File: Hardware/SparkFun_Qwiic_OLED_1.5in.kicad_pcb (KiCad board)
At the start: 2 copper layers, 34.3 x 48.3 mm, 60 parts, among them J1 Qwiic_RA, J2 Qwiic_RA, J3 Conn_01x06, J4 Conn_01x24_FPC, U2 WEO128128ASAP3N00000, U5 AP3012

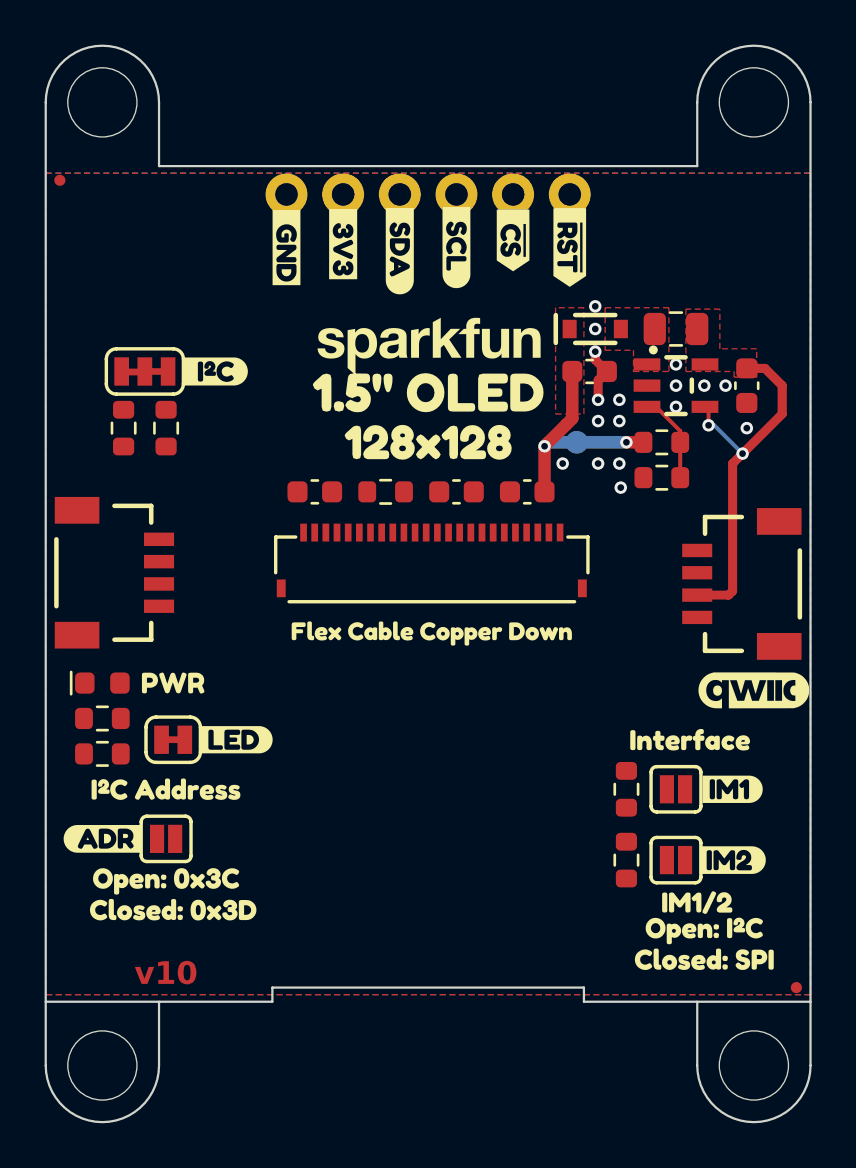
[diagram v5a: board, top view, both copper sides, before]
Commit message: Routes all traces
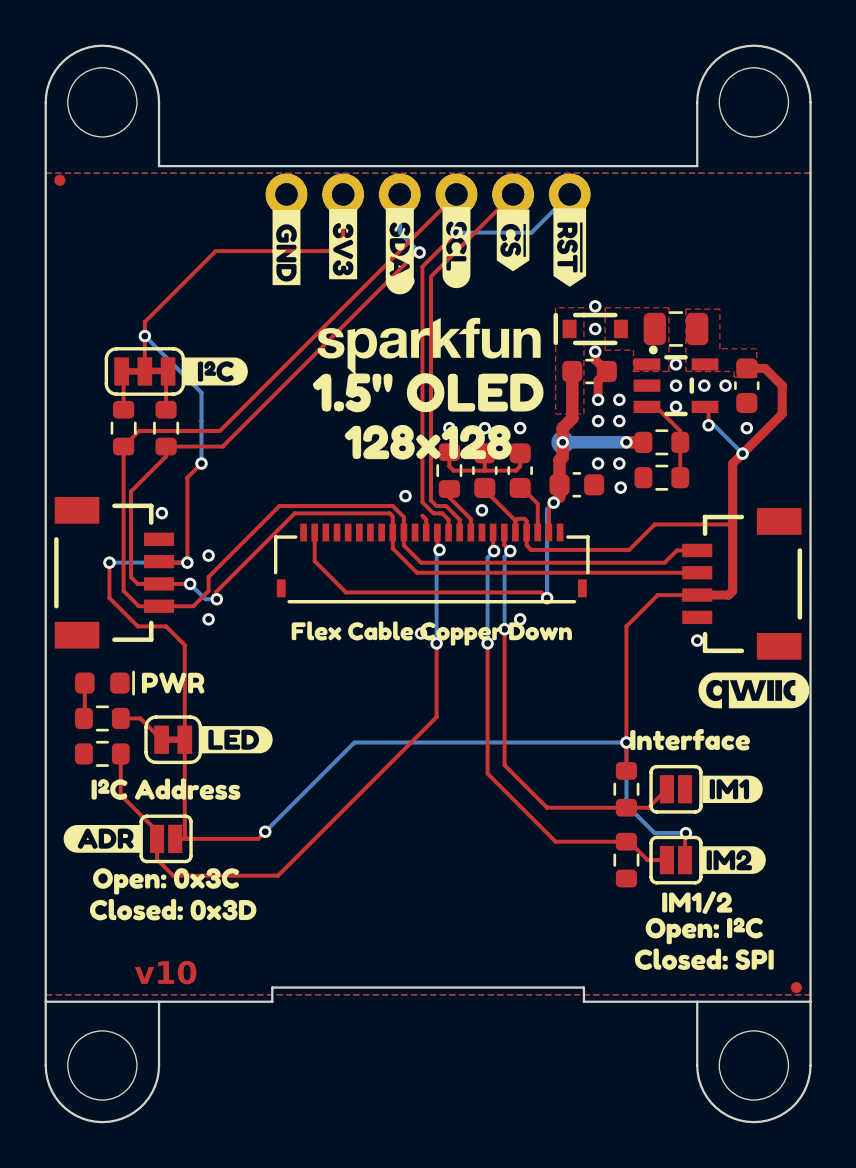
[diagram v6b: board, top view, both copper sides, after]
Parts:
- moved C3 9.26 mm to (144.5, 81.6), turned to 90 degrees
- moved R6 3.01 mm to (141.4, 81.6), turned to -90 degrees
- moved C5 2.25 mm to (147.1, 82.2), turned to 0 degrees
- moved R4 1.91 mm to (128.7, 79.7)
- moved R5 1.91 mm to (126.8, 79.7)
- moved C4 1.59 mm to (143.0, 81.6), turned to 90 degrees
- moved TP1 0.63 mm to (146.4, 80.3)
- turned D1 to 180 degrees
- turned JP2 to 0 degrees
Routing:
- net 3.3V: track 17.1 -> 116.1 mm, vias 2 -> 9
- net SCL/SCK: track 0.00 -> 56.3 mm
- net SDA/SDI: track 0.00 -> 54.1 mm, vias 0 -> 3
- net Net-(J4-Pin_13): track 0.00 -> 29.6 mm, vias 0 -> 2
- net Net-(J4-Pin_18): track 0.00 -> 20.6 mm, vias 0 -> 2
- net ~{RST}: track 0.00 -> 20.6 mm, vias 0 -> 1
- net Net-(J4-Pin_19): track 0.00 -> 19.1 mm, vias 0 -> 2
- net 12V: track 10.1 -> 28.1 mm, vias 2 -> 4
- net ~{CS}: track 0.00 -> 17.6 mm
- net GND: track 2.54 -> 9.07 mm, vias 17 -> 29
- net Net-(J4-Pin_22): track 0.00 -> 2.55 mm
- net Net-(J4-Pin_16): track 0.00 -> 2.35 mm
- net Net-(JP1-A): track 0.00 -> 2.22 mm
- net Net-(JP2-C): track 0.00 -> 1.75 mm
- net Net-(JP2-A): track 0.00 -> 1.75 mm
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
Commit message: Cleans up the routing
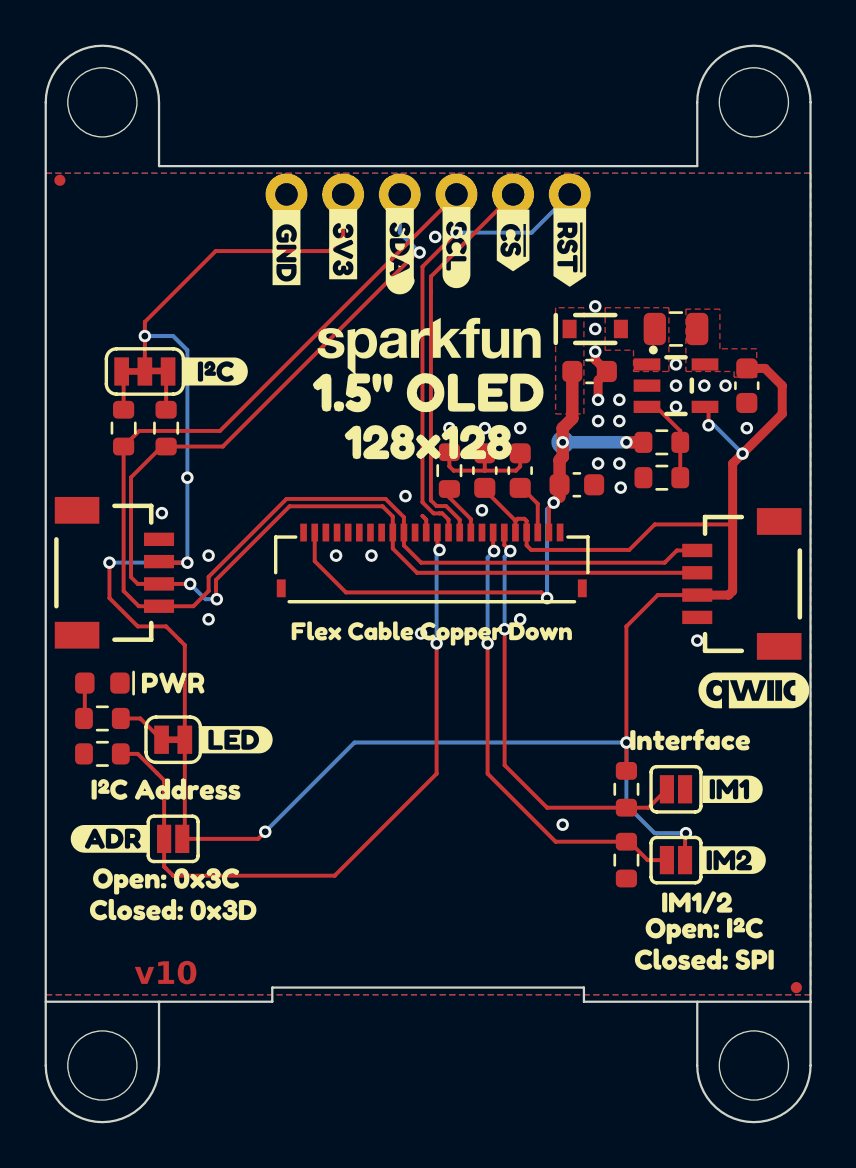
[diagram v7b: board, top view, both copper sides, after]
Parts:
- moved kibuzzard-68100A1E 0.32 mm to (126.1, 98.1)
- moved JP3 0.32 mm to (129.0, 98.1)
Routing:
- net Net-(J4-Pin_13): track 29.6 -> 31.5 mm
- net SDA/SDI: track 54.1 -> 54.8 mm
- net GND: vias 29 -> 33

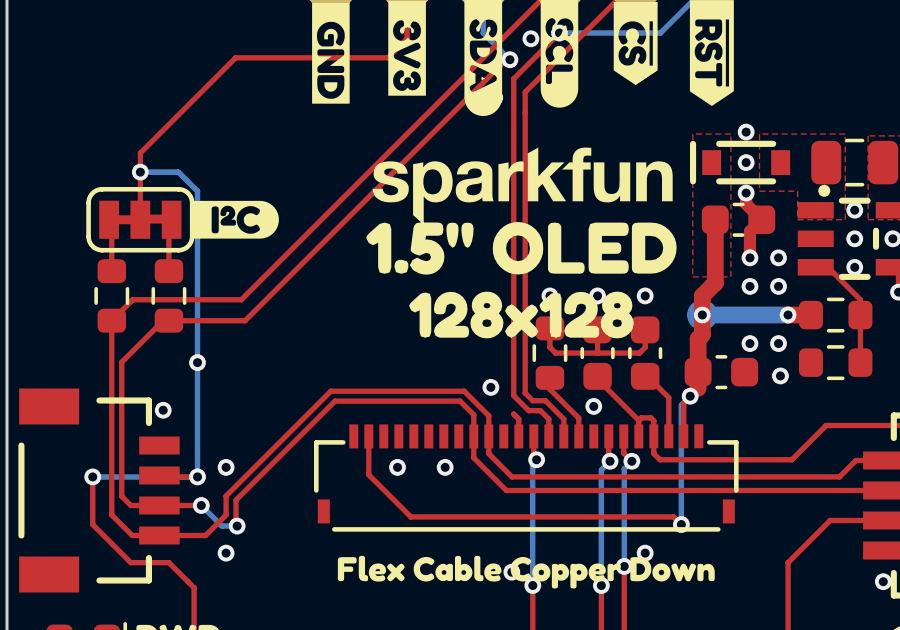
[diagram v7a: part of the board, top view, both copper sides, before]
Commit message: Moves some silk
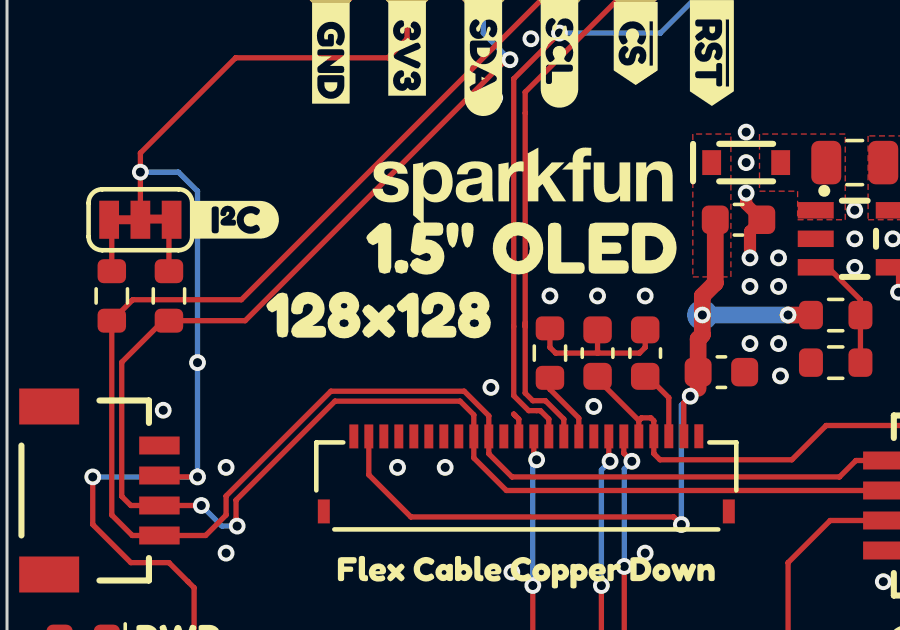
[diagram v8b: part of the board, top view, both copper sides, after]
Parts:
- moved kibuzzard-680FC73E 4.76 mm to (135.6, 80.3)
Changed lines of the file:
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@@
 	(footprint "kibuzzard-680FC73E"
 		(layer "F.Cu")
-		(at 140.411 80.326)
+		(at 135.6485 80.326)
 		(descr "Generated with KiBuzzard")
 		(tags "kb_params=eyJBbGlnbm1lbnRDaG9pY2UiOiAiQ2VudGVyIiwgIkNhcExlZnRDaG9pY2UiOiAiWyIsICJDYXBSaWdodENob2ljZSI6ICIpIiwgIkZvbnRDb21ib0JveCI6ICJGcmVkZHlTcGFyay1SZWd1bGFyIiwgIkhlaWdodEN0cmwiOiAxLjUsICJMYXllckNvbWJvQm94IjogIkYuU2lsa1MiLCAiTGluZVNwYWNpbmdDdHJsIjogMC4zLCAiTXVsdGlMaW5lVGV4dCI6ICIxMjh4MTI4IiwgIlBhZGRpbmdCb3R0b21DdHJsIjogMS4wLCAiUGFkZGluZ0xlZnRDdHJsIjogMi41LCAiUGFkZGluZ1JpZ2h0Q3RybCI6IDIuNSwgIlBhZGRpbmdUb3BDdHJsIjogMS4wLCAiV2lkdGhDdHJsIjogMC4zLCAiYWR2YW5jZWRDaGVja2JveCI6IHRydWUsICJpbmxpbmVGb3JtYXRUZXh0Ym94IjogdHJ1ZSwgImxpbmVvdmVyU3R5bGVDaG9pY2UiOiAiU3F1YXJlIiwgImxpbmVvdmVyVGhpY2tuZXNzQ3RybCI6IDF9")
@@
 		(min_thickness 0.25)
 		(filled_areas_thickness no)
-		(fill
+		(fill yes
 			(thermal_gap 0.5)
 			(thermal_bridge_width 0.5)
@@
 		(min_thickness 0.25)
 		(filled_areas_thickness no)
-		(fill
+		(fill yes
 			(thermal_gap 0.5)
 			(thermal_bridge_width 0.5)
@@
 		(min_thickness 0.25)
 		(filled_areas_thickness no)
-		(fill
+		(fill yes
 			(thermal_gap 0.5)
 			(thermal_bridge_width 0.5)
@@
 		(min_thickness 0.25)
 		(filled_areas_thickness no)
-		(fill
+		(fill yes
 			(thermal_gap 0.254)
 			(thermal_bridge_width 0.4064)
